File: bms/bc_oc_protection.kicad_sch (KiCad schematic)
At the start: 143 parts, among them Q15 MMBT3906, Q16 MMBT3906, Q17 MMBT3906, Q18 MMBT3906, Q19 MMBT3906, Q20 MMBT3906, Q21 MMBT3906, Q22 MMBT3906, Q23 MMBT3906, Q24 MMBT3906, Q25 MMBT3906, Q26 MMBT3906, Q27 A2SHB, Q28 A2SHB, Q29 A2SHB, Q30 A2SHB, Q31 A2SHB, Q32 A2SHB, Q33 MMBT3906, Q34 MMBT3906, Q35 MMBT3906, Q36 MMBT3906, Q37 MMBT3906, Q38 MMBT3906, Q39 MMBT3906, Q40 MMBT3906, Q41 A2SHB, Q42 A2SHB, Q43 A2SHB, Q44 A2SHB, U1 DW01A, U10 HY2213-BB3A, U11 HY2213-BB3A, U12 HY2213-BB3A, U13 DW01A, U14 DW01A, U15 DW01A, U16 DW01A, U17 HY2213-BB3A, U18 HY2213-BB3A, U19 HY2213-BB3A, U2 DW01A, U20 HY2213-BB3A, U3 DW01A, U4 DW01A, U5 DW01A, U6 DW01A, U7 HY2213-BB3A, U8 HY2213-BB3A, U9 HY2213-BB3A

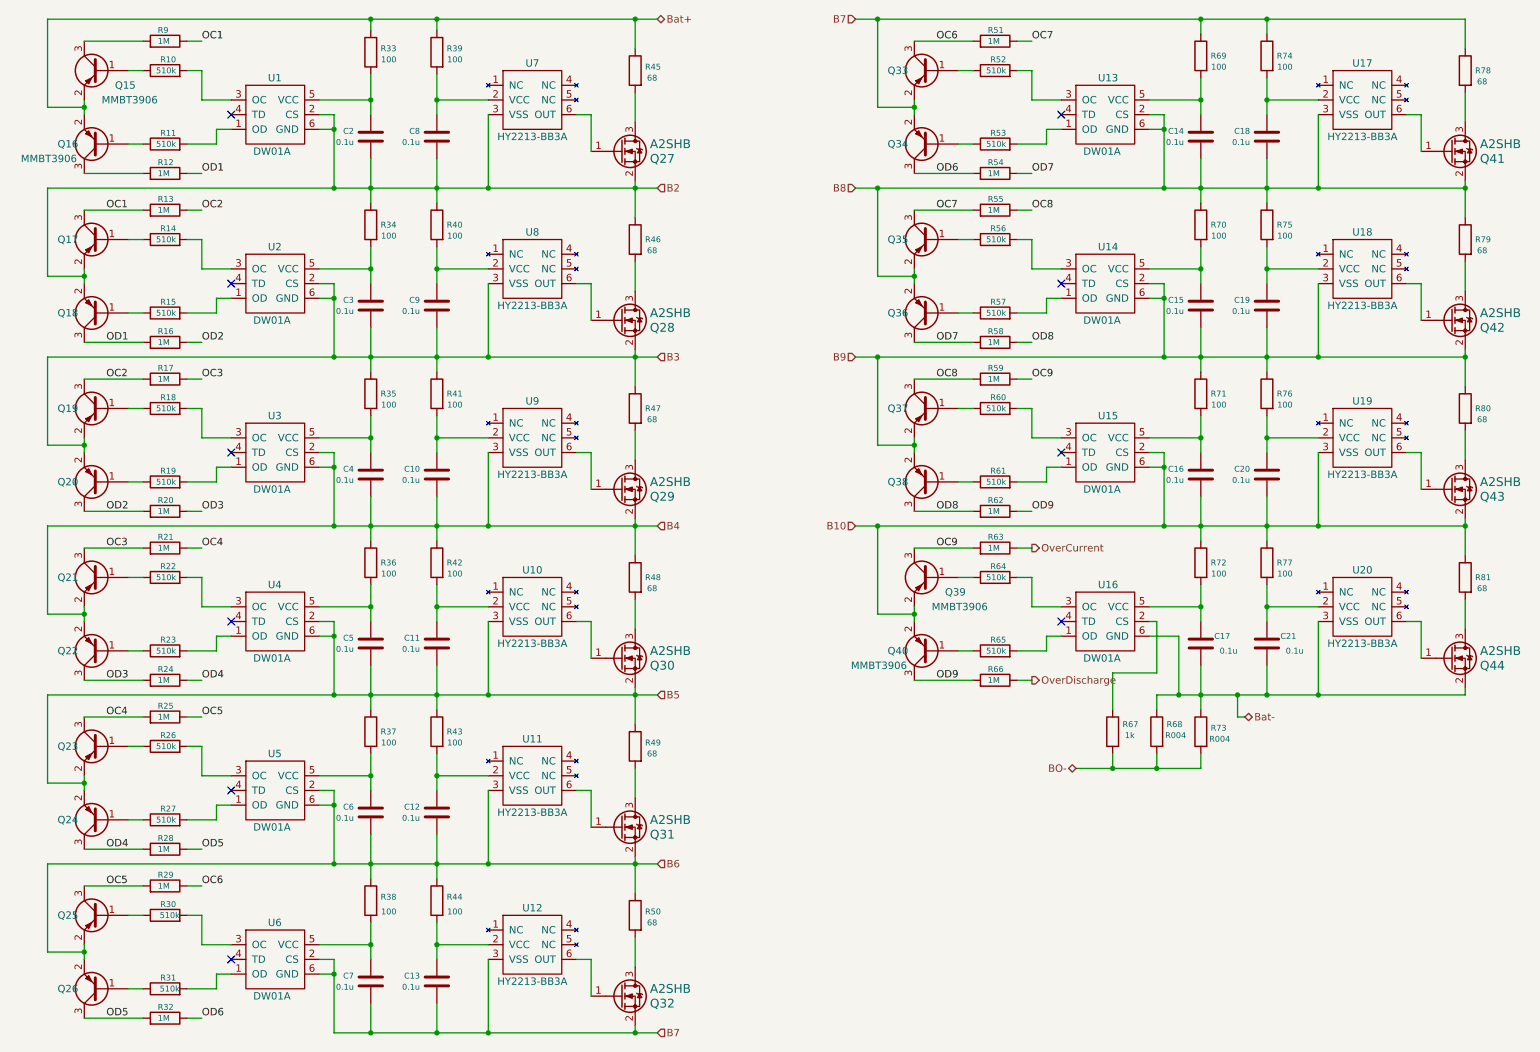
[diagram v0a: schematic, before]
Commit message: bms schematic
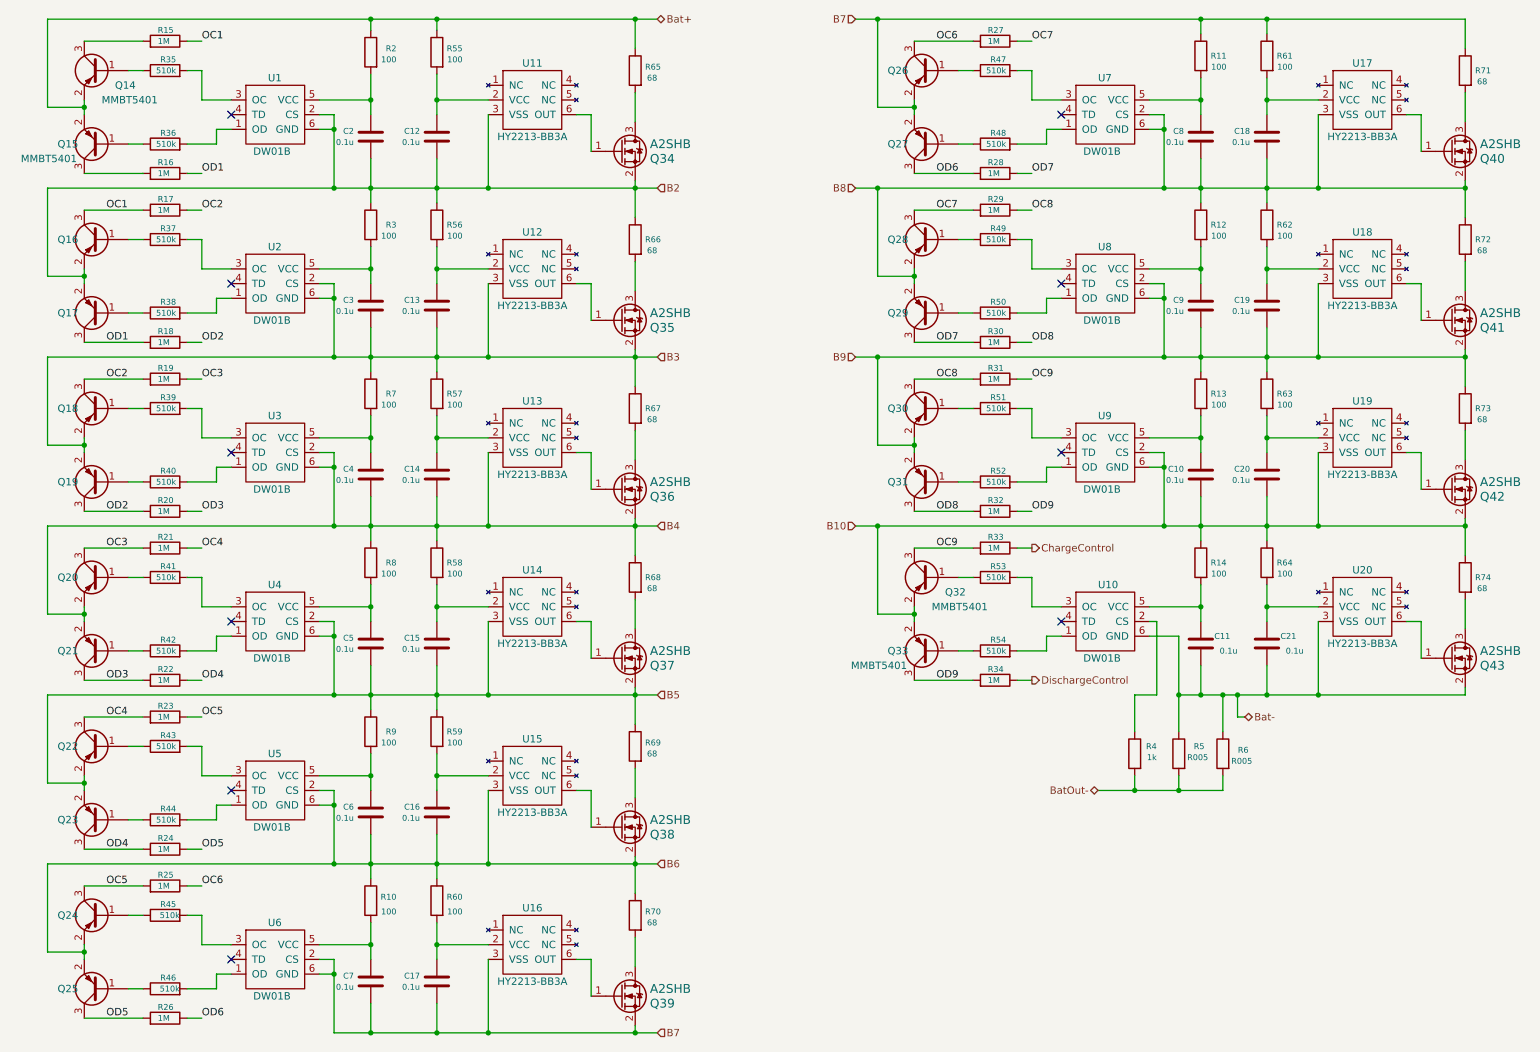
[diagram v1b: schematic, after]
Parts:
- removed R67: 1k, Resistor_SMD:R_0603_1608Metric, symbol Device:R
- removed R68, R73: R004, Resistor_SMD:R_2512_6332Metric, symbol Device:R
- added R4: 1k, Resistor_SMD:R_0603_1608Metric, symbol Device:R
- added R5, R6: R005, Resistor_SMD:R_2512_6332Metric, symbol Device:R
- Q14: renamed from Q15; value MMBT3906 -> MMBT5401
- Q15: renamed from Q16; value MMBT3906 -> MMBT5401
- Q16: renamed from Q17; value MMBT3906 -> MMBT5401
- Q17: renamed from Q18; value MMBT3906 -> MMBT5401
- Q18: renamed from Q19; value MMBT3906 -> MMBT5401
- Q19: renamed from Q20; value MMBT3906 -> MMBT5401
- Q20: renamed from Q21; value MMBT3906 -> MMBT5401
- Q21: renamed from Q22; value MMBT3906 -> MMBT5401
- Q22: renamed from Q23; value MMBT3906 -> MMBT5401
- Q23: renamed from Q24; value MMBT3906 -> MMBT5401
- Q24: renamed from Q25; value MMBT3906 -> MMBT5401
- Q25: renamed from Q26; value MMBT3906 -> MMBT5401
- Q26: renamed from Q33; value MMBT3906 -> MMBT5401
- Q27: renamed from Q34; value MMBT3906 -> MMBT5401
- Q28: renamed from Q35; value MMBT3906 -> MMBT5401
- Q29: renamed from Q36; value MMBT3906 -> MMBT5401
- Q30: renamed from Q37; value MMBT3906 -> MMBT5401
- Q31: renamed from Q38; value MMBT3906 -> MMBT5401
- Q32: renamed from Q39; value MMBT3906 -> MMBT5401
- Q33: renamed from Q40; value MMBT3906 -> MMBT5401
- U1, U2, U3, U4, U5, U6: value DW01A -> DW01B
- U10: renamed from U16; value DW01A -> DW01B
- U7: renamed from U13; value DW01A -> DW01B
- U8: renamed from U14; value DW01A -> DW01B
- U9: renamed from U15; value DW01A -> DW01B
- renumbered C16 to C10, C17 to C11, C8 to C12, C9 to C13, C10 to C14, C11 to C15, C12 to C16, C13 to C17, C14 to C8, C15 to C9, Q27 to Q34, Q28 to Q35, Q29 to Q36, Q30 to Q37, Q31 to Q38, Q32 to Q39, Q41 to Q40, Q42 to Q41, Q43 to Q42, Q44 to Q43, R38 to R10, R69 to R11, R70 to R12, R71 to R13, R72 to R14, R9 to R15, R12 to R16, R13 to R17, R16 to R18, R17 to R19, R33 to R2, R24 to R22, R25 to R23, R28 to R24, R29 to R25, R32 to R26, R51 to R27, R54 to R28, R55 to R29, R34 to R3, R58 to R30, R59 to R31, R62 to R32, R63 to R33, R66 to R34, R10 to R35, R11 to R36, R14 to R37, R15 to R38, R18 to R39, R19 to R40, R22 to R41, R23 to R42, R26 to R43, R27 to R44, R30 to R45, R31 to R46, R52 to R47, R53 to R48, R56 to R49, R57 to R50, R60 to R51, R61 to R52, R64 to R53, R65 to R54, R39 to R55, R40 to R56, R41 to R57, R42 to R58, R43 to R59, R44 to R60, R74 to R61, R75 to R62, R76 to R63, R77 to R64, R45 to R65, R46 to R66, R47 to R67, R48 to R68, R49 to R69, R35 to R7, R50 to R70, R78 to R71, R79 to R72, R80 to R73, R81 to R74, R36 to R8, R37 to R9, U7 to U11, U8 to U12, U9 to U13, U10 to U14, U11 to U15, U12 to U16
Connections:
- net Bat-: now also R5.1, R6.1
- net at U10.2 (CS): now also R4.1
- net OverCurrent renamed ChargeControl
- net OverDischarge renamed DischargeControl
- new net BatOut-: R4.2, R5.2, R6.2
